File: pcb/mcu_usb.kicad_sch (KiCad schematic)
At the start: 33 parts, among them J12 USB_C_Receptacle, J13 UPDI, U10 CP2102N-A02-GQFN24, U11 TLV75533PDBV, U9 AVR128DA48-E/PT, Y1 32.768kHz

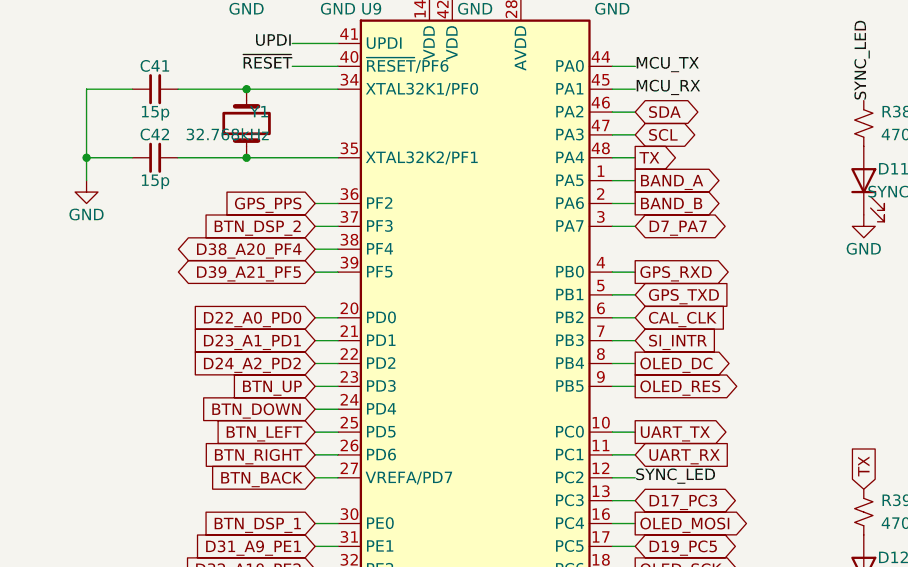
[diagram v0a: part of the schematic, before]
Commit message: GPS_TXD moved to U9 PF5 (pin 39, USART2 RXD ALT1): sch - PB1 NC, R68/HDR_D39 removed, J4.9/D14.3 NC; PCB - GPS_TXD 84 mm west part + new 75 mm east run, torn-up header/LED nets rerouted, HDR_D23 hand-routed, 3 clearance fixes, DRC 0/0; pro netclasses + .NetName DRU + SDA 0.15 mm rule
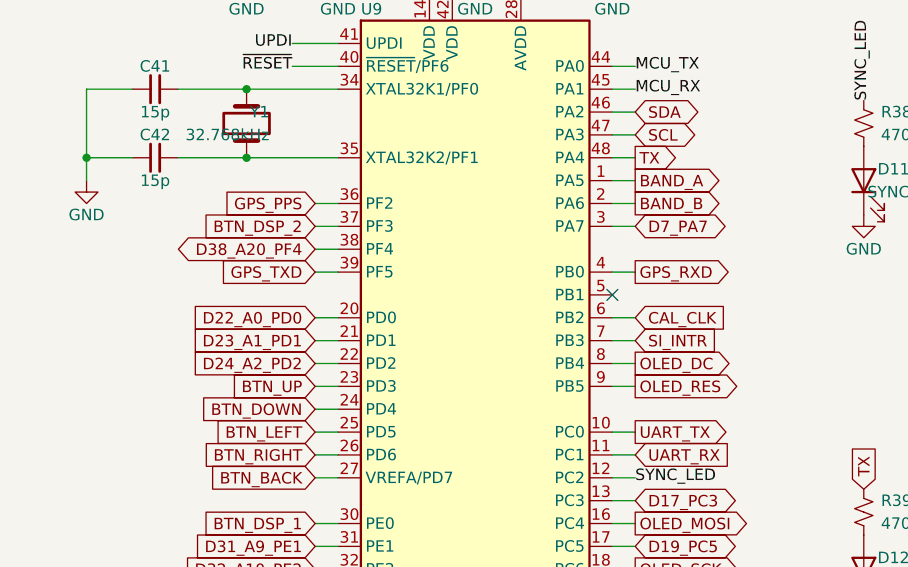
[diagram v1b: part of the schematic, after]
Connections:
- net D39_A21_PF5 is gone; now on net GPS_TXD: U9.39 (PF5)
- net GPS_TXD: no longer U9.5 (PB1)
- no-connect marks 16 -> 17
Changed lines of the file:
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@@
-	(wire
-		(pts
-			(xy 111.76 146.05)
-			(xy 114.3 146.05)
-		)
-		(stroke
-			(width 0)
-			(type default)
-		)
-	)
-	(global_label "GPS_TXD"
-		(shape input)
-		(at 114.3 146.05 0)
-		(fields_autoplaced yes)
-		(effects
-			(font
-				(size 1.27 1.27)
-				(color 0 0 200 1)
-			)
-			(justify left)
-		)
-		(property "Intersheetrefs" "${INTERSHEET_REFS}"
-			(at 114.3 146.05 0)
-			(effects
-				(font
-					(size 1.27 1.27)
-				)
-				(hide yes)
-			)
-		)
-	)
 	(wire
 		(pts
@@
 		)
 	)
-	(global_label "D39_A21_PF5"
-		(shape bidirectional)
+	(global_label "GPS_TXD"
+		(shape input)
 		(at 78.74 143.51 180)
 		(fields_autoplaced yes)
@@
 			(font
 				(size 1.27 1.27)
+				(color 0 0 200 1)
+			)
+			(justify right)
+		)
+		(property "Intersheetrefs" "${INTERSHEET_REFS}"
+			(at 78.74 143.51 0)
+			(effects
+				(font
+					(size 1.27 1.27)
+				)
+				(hide yes)
+			)
+		)
+	)
+	(wire
+		(pts
+			(xy 81.28 173.99) (xy 78.74 173.99)
+		)
+		(stroke
+			(width 0)
+			(type default)
+		)
+	)
+	(global_label "D31_A9_PE1"
+		(shape input)
+		(at 78.74 173.99 180)
+		(fields_autoplaced yes)
+		(effects
+			(font
+				(size 1.27 1.27)
 				(color 0 0 0 1)
 			)
@@
 		)
 		(property "Intersheetrefs" "${INTERSHEET_REFS}"
-			(at 78.74 143.51 0)
-			(effects
-				(font
-					(size 1.27 1.27)
-				)
-				(hide yes)
-			)
-		)
-	)
-	(wire
-		(pts
-			(xy 81.28 173.99) (xy 78.74 173.99)
-		)
-		(stroke
-			(width 0)
-			(type default)
-		)
-	)
-	(global_label "D31_A9_PE1"
-		(shape input)
-		(at 78.74 173.99 180)
+			(at 78.74 173.99 0)
+			(effects
+				(font
+					(size 1.27 1.27)
+				)
+				(hide yes)
+			)
+		)
+	)
+	(wire
+		(pts
+			(xy 81.28 176.53) (xy 78.74 176.53)
+		)
+		(stroke
+			(width 0)
+			(type default)
+		)
+	)
+	(global_label "D32_A10_PE2"
+		(shape input)
+		(at 78.74 176.53 180)
 		(fields_autoplaced yes)
 		(effects
@@
 		)
 		(property "Intersheetrefs" "${INTERSHEET_REFS}"
-			(at 78.74 173.99 0)
-			(effects
-				(font
-					(size 1.27 1.27)
-				)
-				(hide yes)
-			)
-		)
-	)
-	(wire
-		(pts
-			(xy 81.28 176.53) (xy 78.74 176.53)
-		)
-		(stroke
-			(width 0)
-			(type default)
-		)
-	)
-	(global_label "D32_A10_PE2"
-		(shape input)
-		(at 78.74 176.53 180)
+			(at 78.74 176.53 0)
+			(effects
+				(font
+					(size 1.27 1.27)
+				)
+				(hide yes)
+			)
+		)
+	)
+	(wire
+		(pts
+			(xy 81.28 179.07) (xy 78.74 179.07)
+		)
+		(stroke
+			(width 0)
+			(type default)
+		)
+	)
+	(global_label "D33_A11_PE3"
+		(shape input)
+		(at 78.74 179.07 180)
 		(fields_autoplaced yes)
 		(effects
@@
 		)
 		(property "Intersheetrefs" "${INTERSHEET_REFS}"
-			(at 78.74 176.53 0)
-			(effects
-				(font
-					(size 1.27 1.27)
-				)
-				(hide yes)
-			)
-		)
-	)
-	(wire
-		(pts
-			(xy 81.28 179.07) (xy 78.74 179.07)
-		)
-		(stroke
-			(width 0)
-			(type default)
-		)
-	)
-	(global_label "D33_A11_PE3"
-		(shape input)
-		(at 78.74 179.07 180)
-		(fields_autoplaced yes)
-		(effects
-			(font
-				(size 1.27 1.27)
-				(color 0 0 0 1)
-			)
-			(justify right)
-		)
-		(property "Intersheetrefs" "${INTERSHEET_REFS}"
 			(at 78.74 179.07 0)
 			(effects
@@
 		)
 	)
+	(no_connect
+		(at 111.76 146.05)
+	)
 	(sheet_instances

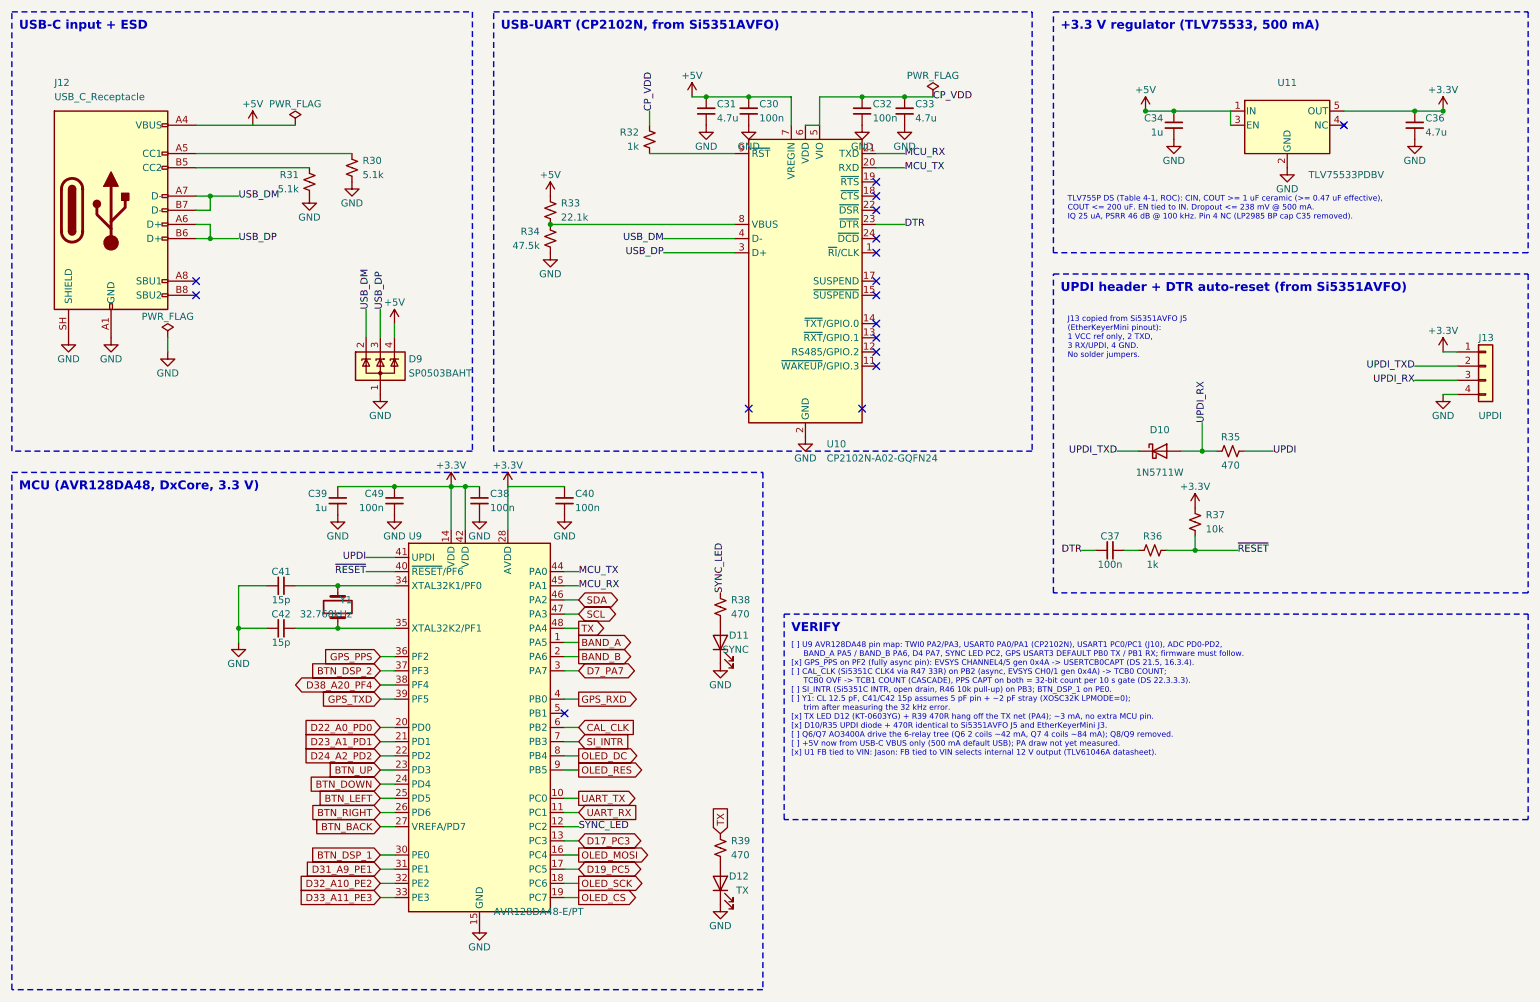
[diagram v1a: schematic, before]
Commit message: Rev C layout: board grown to 130x110 mm, headers J4/J5/J8/J10/J14 removed, power rework layout
- Outline grown 10 mm on top and left edges (130x110 mm); locked edge parts moved with outline
- Removed J4, J5, J8, J10, J14 and support parts (D13-D15, D17, D19, D20, R64-R67, R69-R71, R75-R79); UPDI J13 kept
- Power rework placed and routed (TPS61085 boost, INA193 U14, Q10 soft-start)
- Y1 placed at U9, stray passives moved, silkscreen labels cleaned up
- Routed: DRC 0 errors / 0 unconnected, schematic parity 0, ERC 0; layout gate 11/11
- DRU: ESC_* fine-pitch escape 0.20 mm rule areas, U1 pad-to-pad 0.14 mm
- In2 keep-away waivers (GND-plane shielded): Q2 drain, MCU_TX, MCU_RX near R6, 22.6 mm MCU_RX run near U9
- Libs: 6x6 H13 switch, OLED pin-header module footprint, updated symbols
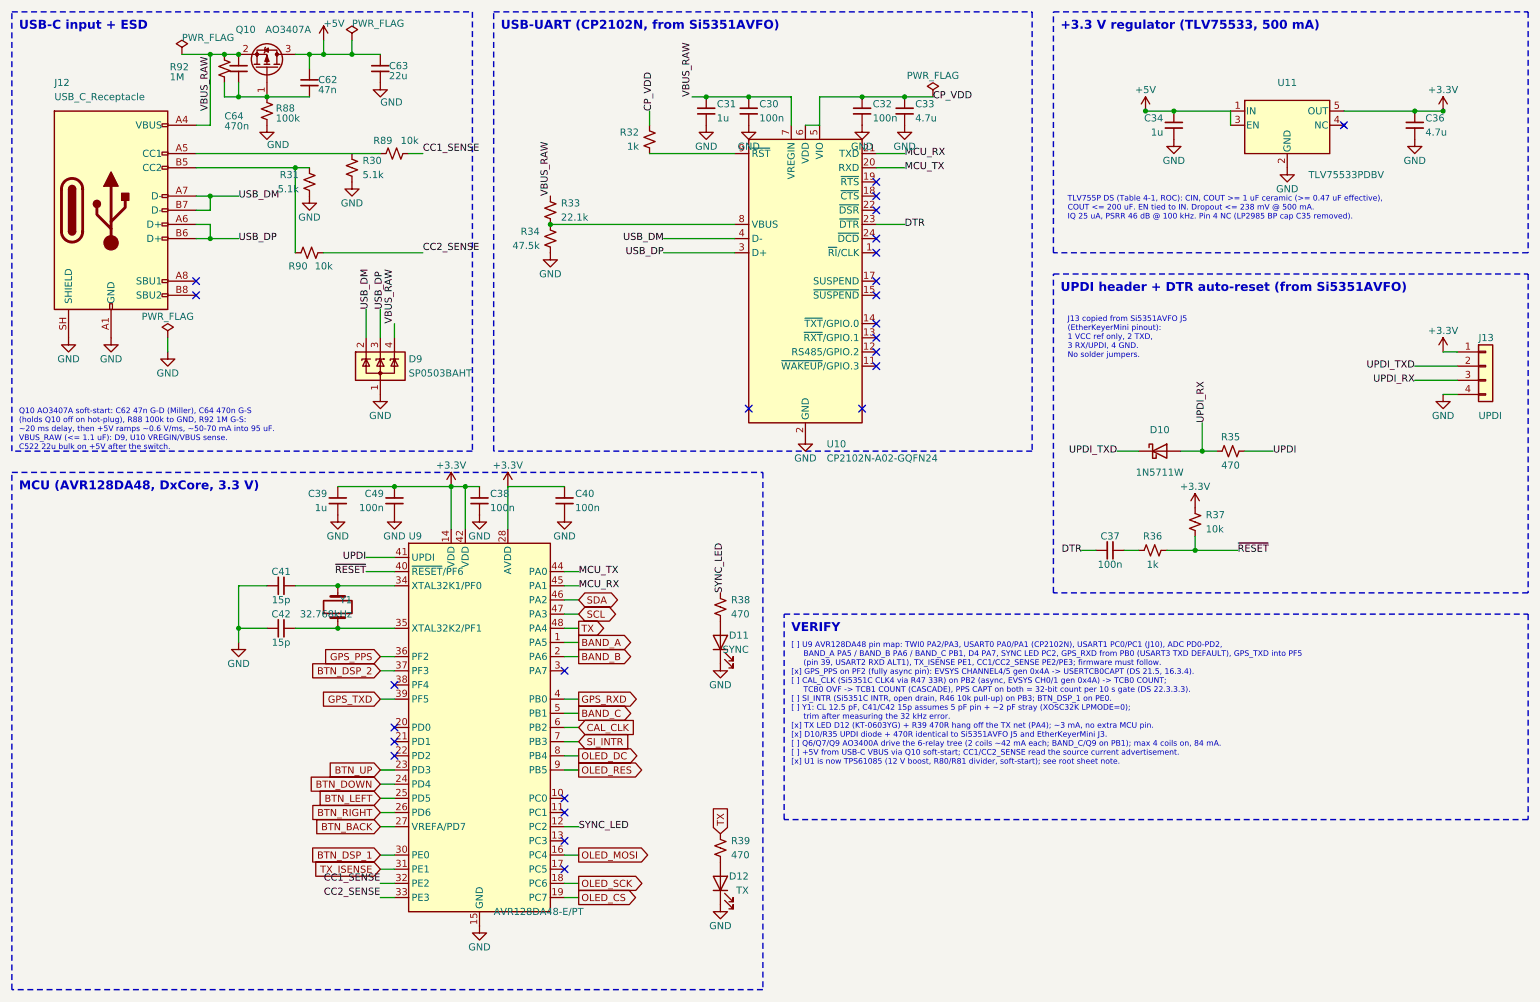
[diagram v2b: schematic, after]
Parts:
- added C62: 47n, Capacitor_SMD:C_0603_1608Metric, symbol Device:C_Small
- added C63: 22u, Capacitor_SMD:C_1206_3216Metric, symbol Device:C_Small
- added C64: 470n, Capacitor_SMD:C_0603_1608Metric, symbol Device:C_Small
- added Q10: AO3407A, Package_TO_SOT_SMD:SOT-23, symbol OpenBeacon2:AO3407A
- added R88: 100k, Resistor_SMD:R_0603_1608Metric, symbol Device:R_Small_US
- added R89, R90: 10k, Resistor_SMD:R_0603_1608Metric, symbol Device:R_Small_US
- added R92: 1M, Resistor_SMD:R_0603_1608Metric, symbol Device:R_Small_US
- C30, C32, C49: footprint Capacitor_SMD:C_0603_1608Metric -> Capacitor_SMD:C_0402_1005Metric; LCSC C14663 -> C1525; MPN CC0603KRX7R9BB104 -> CL05B104KO5NNNC; Manufacturer YAGEO -> Samsung Electro-Mechanics
- C31: value 4.7u -> 1u; footprint Capacitor_SMD:C_0603_1608Metric -> Capacitor_SMD:C_0402_1005Metric; LCSC C19666 -> C15849; MPN CL10A475KO8NNNC -> CL10A105KB8NNNC; Manufacturer Samsung -> Samsung Electro-Mechanics
- C33: footprint Capacitor_SMD:C_0603_1608Metric -> Capacitor_SMD:C_0402_1005Metric; LCSC C19666 -> C23733; MPN CL10A475KO8NNNC -> CL05A475MP5NRNC; Manufacturer Samsung -> Samsung Electro-Mechanics
- C36: footprint Capacitor_SMD:C_0805_2012Metric -> Capacitor_SMD:C_0402_1005Metric; LCSC C1779 -> C23733; MPN CL21A475KAQNNNE -> CL05A475MP5NRNC; Manufacturer Samsung -> Samsung Electro-Mechanics
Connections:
- net +5V: now also C62.1, C63.1, Q10.3 (D); no longer C30.1, C31.1, D9.4 (K), J12.A4 (VBUS), J12.A9 (VBUS), J12.B4 (VBUS), J12.B9 (VBUS), R33.1, U10.7 (VREGIN)
- net GND: now also C63.2, R88.2
- net at J12.B5 (CC2), R31.1: now also R90.1
- net at J12.A5 (CC1), R30.1: now also R89.1
- net BAND_C: now reaches U9.5 (PB1)
- net D17_PC3: no longer names the net of U9.13 (PC3)
- net D19_PC5: no longer names the net of U9.17 (PC5)
- net D22_A0_PD0: no longer names the net of U9.20 (PD0)
- net D23_A1_PD1: no longer names the net of U9.21 (PD1)
- net D24_A2_PD2: no longer names the net of U9.22 (PD2)
- net D31_A9_PE1 renamed TX_ISENSE
- net D32_A10_PE2 renamed CC1_SENSE
- net CC1_SENSE: now also R89.2
- net D33_A11_PE3 renamed CC2_SENSE
- net CC2_SENSE: now also R90.2
- net D38_A20_PF4: no longer names the net of U9.38 (PF4)
- net D7_PA7: no longer names the net of U9.3 (PA7)
- net UART_RX: no longer names the net of U9.11 (PC1)
- net UART_TX: no longer names the net of U9.10 (PC0)
- new net: C62.2, C64.2, Q10.1 (G), R88.1, R92.2
- new net VBUS_RAW: C30.1, C31.1, C64.1, D9.4 (K), J12.A4 (VBUS), J12.A9 (VBUS), J12.B4 (VBUS), J12.B9 (VBUS), Q10.2 (S), R33.1, R92.1, U10.7 (VREGIN)
- no-connect marks 17 -> 25
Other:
- note added: "Q10 AO3407A soft-start: C62 47n G-D (Miller), C64 470n G-S (holds Q10 off on hot-plug), R88 100k to GND, R92 1M G-S: ~20 ms delay, then +5V ramps ~0.6 V/ms, ~50-70 mA into 95 uF. VBUS_RAW (<= 1.1 uF): D9, U10 VREGIN/VBUS sense. C522 22u bulk on +5V after the switch."
- note added: "[ ] U9 AVR128DA48 pin map: TWI0 PA2/PA3, USART0 PA0/PA1 (CP2102N), USART1 PC0/PC1 (J10), ADC PD0-PD2, BAND_A PA5 / BAND_B PA6 / BAND_C PB1, D4 PA7, SYNC LED PC2, GPS_RXD from PB0 (USART3 TXD DEFAULT), GPS_TXD into PF5 (pin 39, USART2 RXD ALT1), TX_ISENSE PE1, CC1/CC2_SENSE PE2/PE3; firmware must follow. [x] GPS_PPS on PF2 (fully async pin): EVSYS CHANNEL4/5 gen 0x4A -> USERTCB0CAPT (DS 21.5, 16.3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"
- note removed: "[ ] U9 AVR128DA48 pin map: TWI0 PA2/PA3, USART0 PA0/PA1 (CP2102N), USART1 PC0/PC1 (J10), ADC PD0-PD2, BAND_A PA5 / BAND_B PA6, D4 PA7, SYNC LED PC2, GPS USART3 DEFAULT PB0 TX / PB1 RX; firmware must follow. [x] GPS_PPS on PF2 (fully async pin): EVSYS CHANNEL4/5 gen 0x4A -> USERTCB0CAPT (DS 21.5, 16.3.4). [ ] CAL_CLK (Si5351C CLK4 via R47 33R) on PB2 (async, EVSYS CH0/1 gen 0x4A) -> TCB0 COUNT; TC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"

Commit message: Renumber all references monotonically 1..N per prefix; sync PCB silk labels and auto-named nets; ERC 0, DRC 0/0
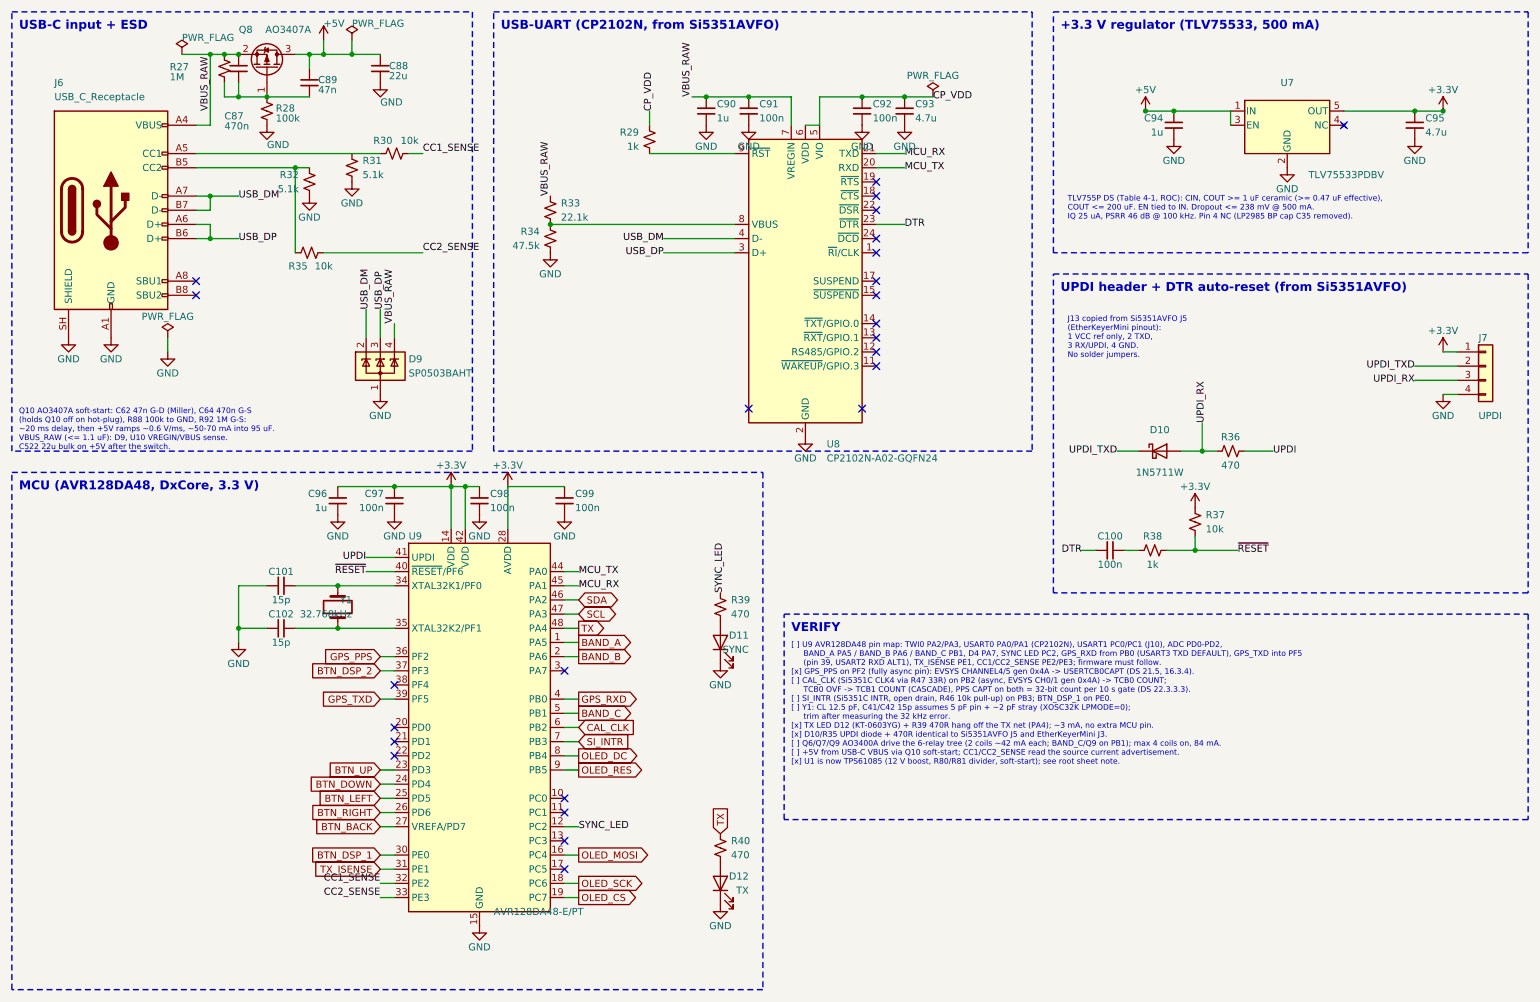
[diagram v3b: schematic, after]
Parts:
- renumbered C37 to C100, C41 to C101, C42 to C102, C64 to C87, C63 to C88, C62 to C89, C31 to C90, C30 to C91, C32 to C92, C33 to C93, C34 to C94, C36 to C95, C39 to C96, C49 to C97, C38 to C98, C40 to C99, J12 to J6, J13 to J7, Q10 to Q8, R92 to R27, R88 to R28, R32 to R29, R89 to R30, R30 to R31, R31 to R32, R90 to R35, R35 to R36, R36 to R38, R38 to R39, R39 to R40, U11 to U7, U10 to U8
